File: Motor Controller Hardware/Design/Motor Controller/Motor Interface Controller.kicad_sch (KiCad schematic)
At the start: 45 parts, among them J7 Controller A NRST, SW1 Controller A Reset, U1 TMC4671-LA, X1 25MHz

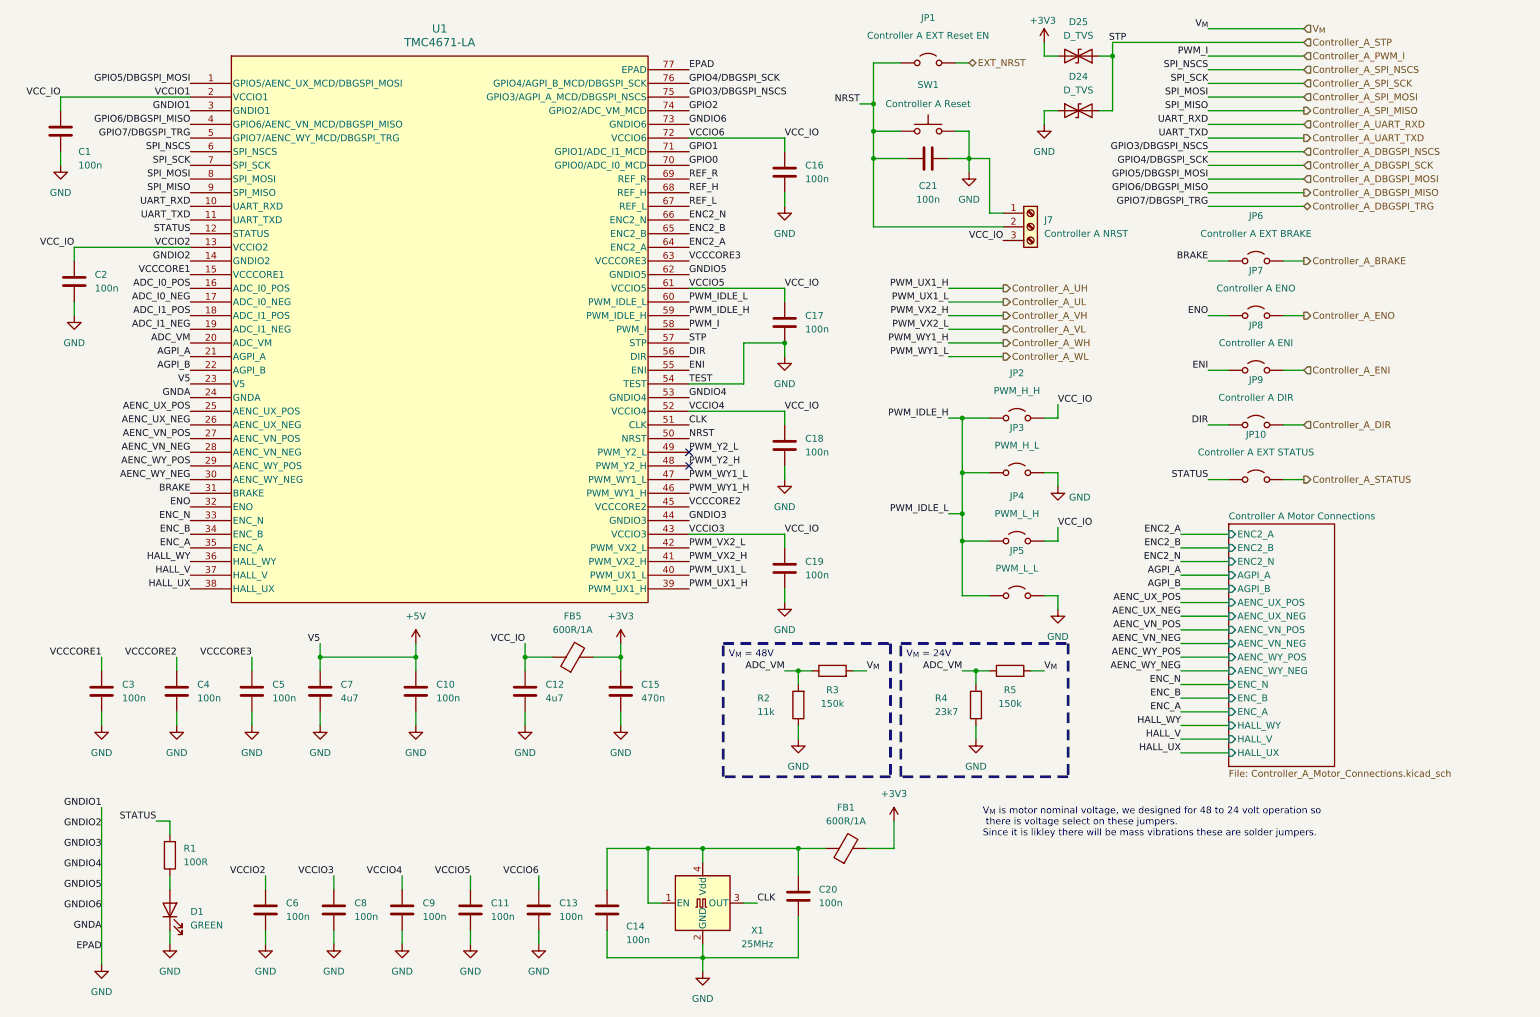
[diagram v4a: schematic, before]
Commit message: Will now just do rev 1 as Silicon mosfets and rev 2 will be gan
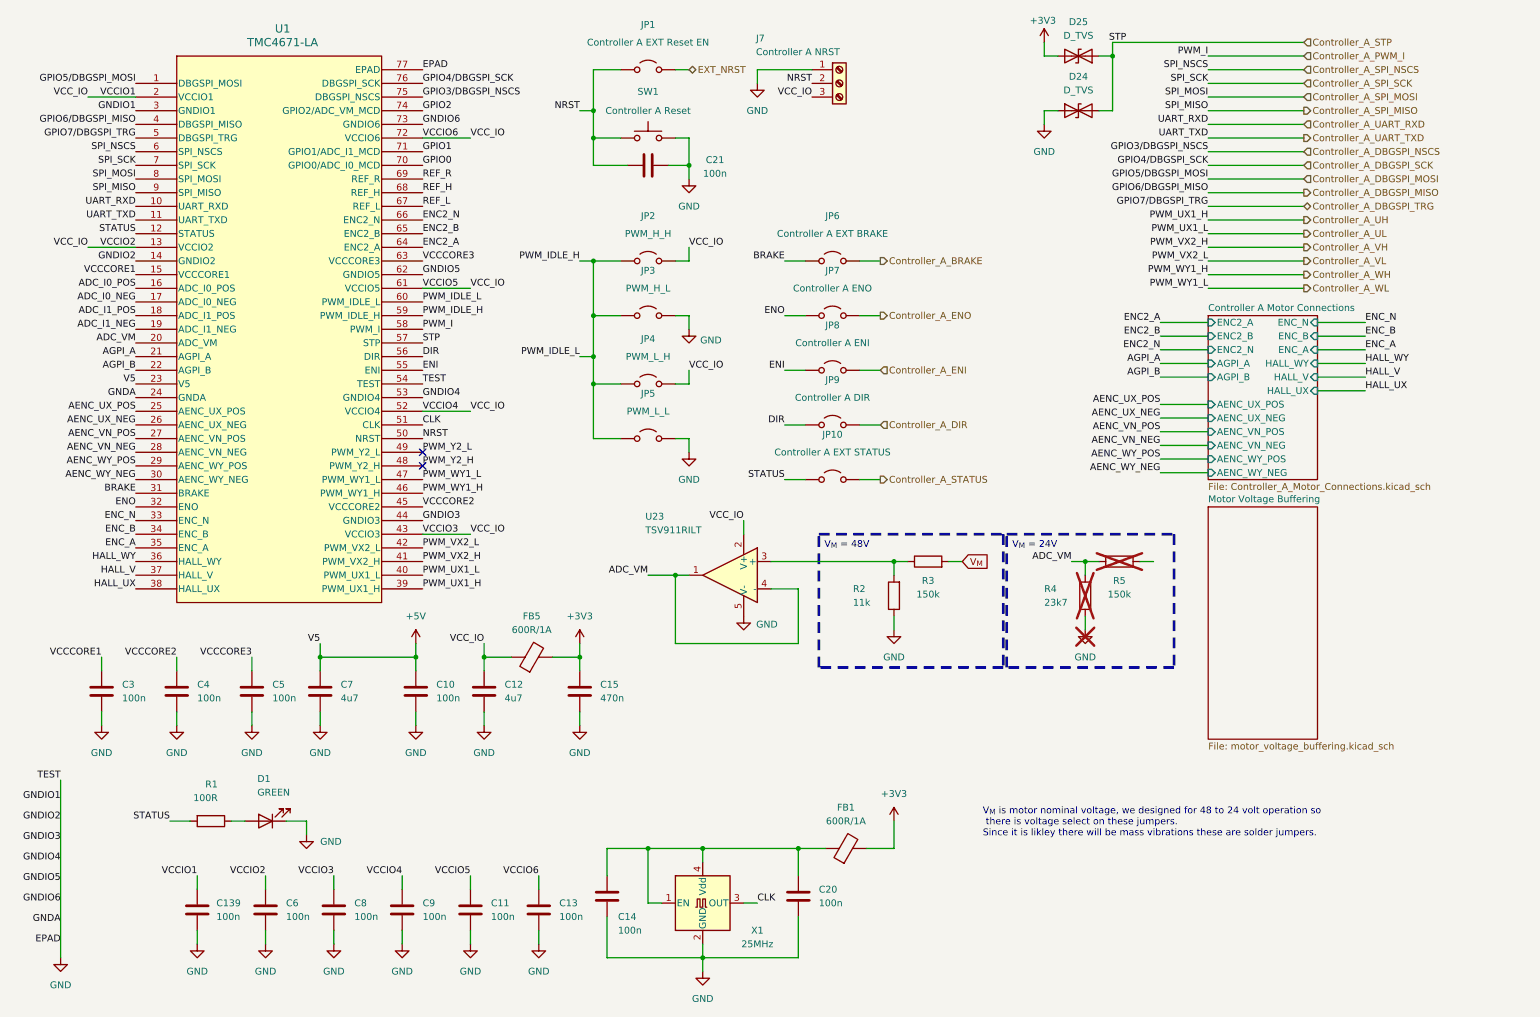
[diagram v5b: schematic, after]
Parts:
- removed C1, C16, C17, C18, C19, C2: 100n, Capacitor_SMD:C_0603_1608Metric, symbol Device:C
- added C139: 100n, Capacitor_SMD:C_0603_1608Metric, symbol Device:C
- added U23: TSV911RILT, Package_TO_SOT_SMD:SOT-23-5, symbol Amplifier_Operational:TSV911RILT
- R4, R5: now not fitted; now left out of the parts list
- SW1: footprint (none) -> Button_Switch_THT:SW_PUSH_6mm
- U1: footprint ecocad:QFN76_10P5X6P5_TRI -> (none)
- X1: footprint Oscillator:Oscillator_SMD_Abracon_ASE-4Pin_3.2x2.5mm -> Oscillator:Oscillator_SMD_SeikoEpson_SG8002CE-4Pin_3.2x2.5mm; DK# (none) -> 114-SG3225CAN25.0000M-TJGA6CT-ND
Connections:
- net ADC_VM: now also U23.1, U23.4 (-); no longer R2.2, R3.1
- net GND: now also C139.2, U23.5 (V-)
- net VCCIO1: now also C139.1, U23.2 (V+)
- net V_{M}: no longer R5.2
- new net: R2.2, R3.1, U23.3 (+)
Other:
- added sheet Motor Voltage Buffering (motor_voltage_buffering.kicad_sch)
- moved on the sheet: C12, C14, C15, C21, D1, FB5, J7, JP1, JP10, JP2, JP3, JP4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

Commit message: A
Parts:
- U1: footprint (none) -> ecocad:QFN76_10P5X6P5_TRI
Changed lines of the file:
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@@
 			)
 		)
-		(property "Footprint" ""
+		(property "Footprint" "ecocad:QFN76_10P5X6P5_TRI"
 			(at 60.706 7.366 0)
 			(effects

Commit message: Arranged most footprints will route soon
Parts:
- U1: LCSC Part# (none) -> C465954

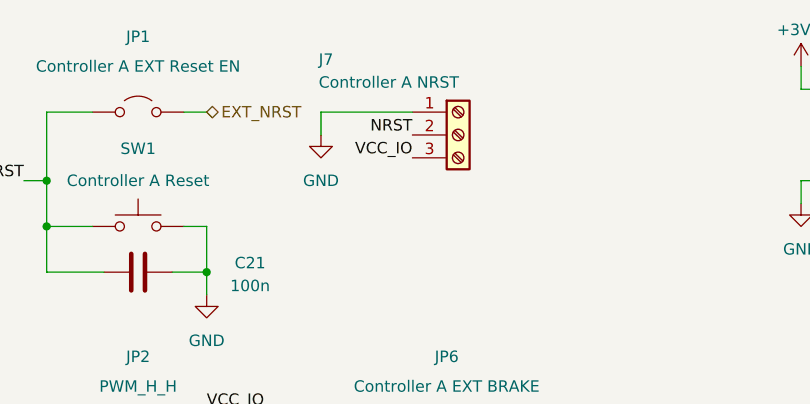
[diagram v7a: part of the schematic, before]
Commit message: made some layout changes and started routing power stage
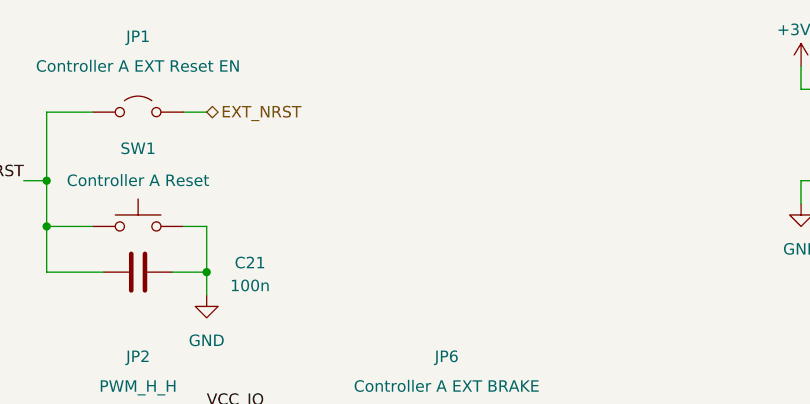
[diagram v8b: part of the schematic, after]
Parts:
- removed J7: Controller A NRST, TerminalBlock_Phoenix:TerminalBlock_Phoenix_MPT-0,5-3-2.54_1x03_P2.54mm_Horizontal, symbol Connector:Screw_Terminal_01x03
- JP1, JP10, JP2, JP3, JP4, JP5, JP6, JP7, JP8, JP9: footprint Connector_PinHeader_2.54mm:PinHeader_1x02_P2.54mm_Vertical -> Jumper:SolderJumper-2_P1.3mm_Open_TrianglePad1.0x1.5mm
- U1: footprint ecocad:QFN76_10P5X6P5_TRI -> ecocad_lib_footprints:QFN76_10P5X6P5_TRI
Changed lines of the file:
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@@
 	(wire
 		(pts
-			(xy 149.86 25.4) (xy 149.86 22.86)
-		)
-		(stroke
-			(width 0)
-			(type default)
-		)
-	)
-	(wire
-		(pts
 			(xy 55.88 132.08) (xy 55.88 134.62)
 		)
@@
 	(wire
 		(pts
-			(xy 149.86 22.86) (xy 160.02 22.86)
-		)
-		(stroke
-			(width 0)
-			(type default)
-		)
-	)
-	(wire
-		(pts
 			(xy 152.4 114.3) (xy 175.26 114.3)
 		)
@@
 		)
 	)
-	(label "NRST"
-		(at 160.02 25.4 180)
-		(fields_autoplaced yes)
-		(effects
-			(font
-				(size 1.27 1.27)
-			)
-			(justify right bottom)
-		)
-	)
 	(label "HALL_V"
 		(at 262.89 80.01 0)
@@
 		)
 	)
-	(label "VCC_IO"
-		(at 160.02 27.94 180)
-		(fields_autoplaced yes)
-		(effects
-			(font
-				(size 1.27 1.27)
-			)
-			(justify right bottom)
-		)
-	)
 	(label "V5"
 		(at 68.58 129.54 180)
@@
 			)
 		)
-		(property "Footprint" "Connector_PinHeader_2.54mm:PinHeader_1x02_P2.54mm_Vertical"
+		(property "Footprint" "Jumper:SolderJumper-2_P1.3mm_Open_TrianglePad1.0x1.5mm"
 			(at 163.83 58.42 0)
 			(effects
@@
 			)
 		)
-		(property "Footprint" "Connector_PinHeader_2.54mm:PinHeader_1x02_P2.54mm_Vertical"
+		(property "Footprint" "Jumper:SolderJumper-2_P1.3mm_Open_TrianglePad1.0x1.5mm"
 			(at 163.83 88.9 0)
 			(effects
@@
 			)
 		)
-		(property "Footprint" "Connector_PinHeader_2.54mm:PinHeader_1x02_P2.54mm_Vertical"
+		(property "Footprint" "Jumper:SolderJumper-2_P1.3mm_Open_TrianglePad1.0x1.5mm"
 			(at 129.54 58.42 0)
 			(effects
@@
 	)
 	(symbol
-		(lib_id "power:GND")
-		(at 149.86 25.4 0)
-		(unit 1)
-		(exclude_from_sim no)
-		(in_bom yes)
-		(on_board yes)
-		(dnp no)
-		(fields_autoplaced yes)
-		(property "Reference" "#PWR02"
-			(at 149.86 31.75 0)
-			(effects
-				(font
-					(size 1.27 1.27)
-				)
-				(hide yes)
-			)
-		)
-		(property "Value" "GND"
-			(at 149.86 30.48 0)
-			(effects
-				(font
-					(size 1.27 1.27)
-				)
-			)
-		)
-		(property "Footprint" ""
-			(at 149.86 25.4 0)
-			(effects
-				(font
-					(size 1.27 1.27)
-				)
-				(hide yes)
-			)
-		)
-		(property "Datasheet" ""
-			(at 149.86 25.4 0)
-			(effects
-				(font
-					(size 1.27 1.27)
-				)
-				(hide yes)
-			)
-		)
-		(property "Description" "Power symbol creates a global label with name \"GND\" , ground"
-			(at 149.86 25.4 0)
-			(effects
-				(font
-					(size 1.27 1.27)
-				)
-				(hide yes)
-			)
-		)
-		(pin "1"
-		)
-		(instances
-			(project "Motor Controller"
-				(path "/480a1464-7c70-42e1-b2f7-69e659e11383/61655235-6b41-44b9-81da-f6727ca7c811"
-					(reference "#PWR02")
-					(unit 1)
-				)
-			)
-		)
-	)
-	(symbol
 		(lib_id "Amplifier_Operational:TSV911RILT")
 		(at 144.78 116.84 0)
@@
 			)
 		)
-		(property "Footprint" "Connector_PinHeader_2.54mm:PinHeader_1x02_P2.54mm_Vertical"
+		(property "Footprint" "Jumper:SolderJumper-2_P1.3mm_Open_TrianglePad1.0x1.5mm"
 			(at 129.54 68.58 0)
 			(effects
@@
 			)
 		)
-		(property "Footprint" "Connector_PinHeader_2.54mm:PinHeader_1x02_P2.54mm_Vertical"
+		(property "Footprint" "Jumper:SolderJumper-2_P1.3mm_Open_TrianglePad1.0x1.5mm"
 			(at 163.83 99.06 0)
 			(effects
@@
 			)
 		)
-		(property "Footprint" "ecocad:QFN76_10P5X6P5_TRI"
+		(property "Footprint" "ecocad_lib_footprints:QFN76_10P5X6P5_TRI"
 			(at 60.706 7.366 0)
 			(effects
@@
 			)
 		)
-		(property "Footprint" "Connector_PinHeader_2.54mm:PinHeader_1x02_P2.54mm_Vertical"
+		(property "Footprint" "Jumper:SolderJumper-2_P1.3mm_Open_TrianglePad1.0x1.5mm"
 			(at 129.54 91.44 0)
 			(effects
@@
 			)
 		)
-		(property "Footprint" "Connector_PinHeader_2.54mm:PinHeader_1x02_P2.54mm_Vertical"
+		(property "Footprint" "Jumper:SolderJumper-2_P1.3mm_Open_TrianglePad1.0x1.5mm"
 			(at 129.54 22.86 0)
 			(effects
@@
 			)
 		)
-		(property "Footprint" "Connector_PinHeader_2.54mm:PinHeader_1x02_P2.54mm_Vertical"
+		(property "Footprint" "Jumper:SolderJumper-2_P1.3mm_Open_TrianglePad1.0x1.5mm"
 			(at 163.83 68.58 0)
 			(effects
@@
 	)
 	(symbol
-		(lib_id "Connector:Screw_Terminal_01x03")
-		(at 165.1 25.4 0)
-		(unit 1)
-		(exclude_from_sim no)
-		(in_bom yes)
-		(on_board yes)
-		(dnp no)
-		(property "Reference" "J7"
-			(at 149.606 17.018 0)
-			(effects
-				(font
-					(size 1.27 1.27)
-				)
-				(justify left)
-			)
-		)
-		(property "Value" "Controller A NRST"
-			(at 149.606 19.558 0)
-			(effects
-				(font
-					(size 1.27 1.27)
-				)
-				(justify left)
-			)
-		)
-		(property "Footprint" "TerminalBlock_Phoenix:TerminalBlock_Phoenix_MPT-0,5-3-2.54_1x03_P2.54mm_Horizontal"
-			(at 165.1 25.4 0)
-			(effects
-				(font
-					(size 1.27 1.27)
-				)
-				(hide yes)
-			)
-		)
-		(property "Datasheet" "~"
-			(at 165.1 25.4 0)
-			(effects
-				(font
-					(size 1.27 1.27)
-				)
-				(hide yes)
-			)
-		)
-		(property "Description" "Generic screw terminal, single row, 01x03, script generated (kicad-library-utils/schlib/autogen/connector/)"
-			(at 165.1 25.4 0)
-			(effects
-				(font
-					(size 1.27 1.27)
-				)
-				(hide yes)
-			)
-		)
-		(property "LCSC Part#" ""
-			(at 165.1 25.4 0)
-			(effects
-				(font
-					(size 1.27 1.27)
-				)
-				(hide yes)
-			)
-		)
-		(pin "3"
-		)
-		(pin "1"
-		)
-		(pin "2"
-		)
-		(instances
-			(project "Motor Controller"
-				(path "/480a1464-7c70-42e1-b2f7-69e659e11383/61655235-6b41-44b9-81da-f6727ca7c811"
-					(reference "J7")
-					(unit 1)
-				)
-			)
-		)
-	)
-	(symbol
 		(lib_id "Jumper:Jumper_2_Open")
 		(at 163.83 78.74 0)
@@
 			)
 		)
-		(property "Footprint" "Connector_PinHeader_2.54mm:PinHeader_1x02_P2.54mm_Vertical"
+		(property "Footprint" "Jumper:SolderJumper-2_P1.3mm_Open_TrianglePad1.0x1.5mm"
 			(at 163.83 78.74 0)
 			(effects
@@
 			)
 		)
-		(property "Footprint" "Connector_PinHeader_2.54mm:PinHeader_1x02_P2.54mm_Vertical"
+		(property "Footprint" "Jumper:SolderJumper-2_P1.3mm_Open_TrianglePad1.0x1.5mm"
 			(at 129.54 81.28 0)
 			(effects
